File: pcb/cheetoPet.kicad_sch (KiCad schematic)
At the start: 90 parts, among them J1 bat connector, J2 USB_C_Receptacle_USB2.0_16P, Q1 FS8205A, Q2 BSS138, SW10 RESET, SW6 POWER, SW7 B, SW8 A, SW9 X, U1 USBLC6-2SC6, U10 TPS63802DLAR, U11 KLJ-01304T-08R07W, U2 MAX98357A, U3 DW01A, U4 BQ24074RGT, U5 MAX17048G_T10, U6 LSM6DSL, U7 RV-3028-C7, U8 ESP32-S3-MINI-1U, U9 WS-003DB

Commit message: pcb finished
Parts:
- removed FPC1: FPC-05FB-12PH20, EasyEDA:FPC-SMD_12P-P0.50_XUNPU_FPC-05FB-12PH20, symbol EasyEDA:FPC-05FB-12PH20
- removed J1: bat connector, Connector_PinHeader_2.00mm:PinHeader_1x02_P2.00mm_Vertical, symbol Connector:Conn_01x02_Socket
- removed SW6: POWER, EasyEDA:SW-SMD_5P-L4.2-W2.8-P1.60-LS4.6-TR, symbol EasyEDA:KMR223GLFG
- added C25: 100nF, Capacitor_SMD:C_0402_1005Metric, symbol Device:C
- added C26: 0.1uF, Capacitor_SMD:C_0402_1005Metric, symbol Device:C_Small
- added C27, C28: 22uF, Capacitor_SMD:C_0805_2012Metric, symbol Device:C
- added CN1: bat connector, EasyEDA:CONN-SMD_P2.00_S2B-PH-SM4-TB-LF-SN, symbol EasyEDA:S2B-PH-SM4-TB
- added FPC1: FPC-05F-12PH20, EasyEDA:FPC-SMD_12P-P0.50_FPC-05F-12PH20, symbol EasyEDA:FPC-05F-12PH20
- added SW1: POWER, EasyEDA:SW-SMD_LXTD-0204-034, symbol EasyEDA:LXTD-0204-034
- C1, C11, C17, C19, C5, C6, C7: LCSC Part (none) -> C1525
- C10, C14, C22, C23: LCSC Part (none) -> C45783
- C12, C2, C20, C3, C8, C9: LCSC Part (none) -> C19702
- C15, C16, C18, C21, C24: footprint Capacitor_SMD:C_0603_1608Metric -> Capacitor_SMD:C_0402_1005Metric; LCSC Part (none) -> C1525
- C4: LCSC Part (none) -> C52923
- F1: LCSC Part (none) -> C2649901
- J2: LCSC Part (none) -> C2988369
- L1: LCSC Part (none) -> C42455362
- Q1: LCSC Part (none) -> C908265
- Q2: LCSC Part (none) -> C7420339
- R1: LCSC Part (none) -> C25076
- R10: LCSC Part (none) -> C42396634
- R11: LCSC Part (none) -> C25762
- R12, R13, R15, R16, R17, R18, R22, R23, R24, R25, R26, R27, R31, R32, R35, R38, R5, R8: LCSC Part (none) -> C25744
- R19, R20: LCSC Part (none) -> C25900
- R2: LCSC Part (none) -> C11702
- R21: LCSC Part (none) -> C25077
- R28, R29, R30, R33, R34: LCSC Part (none) -> C25092
- R3, R4: LCSC Part (none) -> C25905
- R36: LCSC Part (none) -> C144750
- R37: LCSC Part (none) -> C2909393
- R6: LCSC Part (none) -> C17168
- R7: LCSC Part (none) -> C25867
- R9: LCSC Part (none) -> C852602
- TP1, TP2, TP3, TP4, TP5, TP6, TP7: now not fitted; now left out of the parts list
- U1: LCSC Part (none) -> C5180249
- U2: LCSC Part (none) -> C910544
- U3: LCSC Part (none) -> C42380662
- U4: LCSC Part (none) -> C54313
- U5: footprint MAX17048G_T10:SON50P200X200X80-9N -> Package_DFN_QFN:TDFN-8-1EP_2x2mm_P0.5mm_EP0.8x1.2mm; LCSC Part (none) -> C2682616
- U6: LCSC Part (none) -> C126672
- U7: LCSC Part (none) -> C3019759
- U8: LCSC Part (none) -> C2980299
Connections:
- net +3V3: now also C27.2, FPC1.8, FPC1.9
- net BAT+: now also CN1.1
- net BAT-: now also CN1.2
- net CHG: now also U8.27 (IO47)
- net DAC_BCLK: now also U8.21 (IO17); no longer U8.37 (IO41)
- net DAC_LRCLK: now also U8.22 (IO18); no longer U8.38 (IO42)
- net DAC_SD: now also U8.17 (IO13); no longer U8.30 (IO48)
- net EN: now also C25.1
- net GND: now also C25.2, C26.1, C27.1, C28.2, FPC1.12, FPC1.13, FPC1.14, FPC1.2, SW1.2
- net POWER: now also SW1.1
- net ROCK_L: now also U8.37 (IO41); no longer U8.21 (IO17)
- net ROCK_R: now also U8.38 (IO42); no longer U8.22 (IO18)
- net TFT_DC: now also FPC1.3
- net TFT_RES: now also FPC1.4
- net TFT_TE: now also FPC1.1
- net at R21.1: now also C26.2, C28.1, FPC1.10
- net at Q2.3 (D): now also FPC1.11
- net at R29.1: now also FPC1.5
- net at R28.1: now also FPC1.6
- net at R30.1: now also FPC1.7
- no-connect marks 27 -> 30
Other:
- moved on the sheet: R21, R26

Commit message: merged kidna with like uhhh some stuff
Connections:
- net +3V3: now also SW9.3
- net GND: no longer SW9.3
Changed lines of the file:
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@@
 	)
 	(symbol
+		(lib_id "power:+3V3")
+		(at 120.65 191.77 180)
+		(unit 1)
+		(body_style 1)
+		(exclude_from_sim no)
+		(in_bom yes)
+		(on_board yes)
+		(in_pos_files yes)
+		(dnp no)
+		(property "Reference" "#PWR053"
+			(at 120.65 187.96 0)
+			(hide yes)
+			(show_name no)
+			(do_not_autoplace no)
+			(effects
+				(font
+					(size 1.27 1.27)
+				)
+			)
+		)
+		(property "Value" "+3V3"
+			(at 120.65 195.326 0)
+			(show_name no)
+			(do_not_autoplace no)
+			(effects
+				(font
+					(size 1.27 1.27)
+				)
+			)
+		)
+		(property "Footprint" ""
+			(at 120.65 191.77 0)
+			(hide yes)
+			(show_name no)
+			(do_not_autoplace no)
+			(effects
+				(font
+					(size 1.27 1.27)
+				)
+			)
+		)
+		(property "Datasheet" ""
+			(at 120.65 191.77 0)
+			(hide yes)
+			(show_name no)
+			(do_not_autoplace no)
+			(effects
+				(font
+					(size 1.27 1.27)
+				)
+			)
+		)
+		(property "Description" "Power symbol creates a global label with name \"+3V3\""
+			(at 120.65 191.77 0)
+			(hide yes)
+			(show_name no)
+			(do_not_autoplace no)
+			(effects
+				(font
+					(size 1.27 1.27)
+				)
+			)
+		)
+		(pin "1"
+		)
+		(instances
+			(project "cheetoPet"
+				(path "/2746c69b-027c-4aec-b1d7-a024d4e17723"
+					(reference "#PWR053")
+					(unit 1)
+				)
+			)
+		)
+	)
+	(symbol
 		(lib_id "power:GND")
 		(at 359.41 143.51 0)
@@
 					(unit 1)
 				)
-			)
-		)
-	)
-	(symbol
-		(lib_id "power:GND")
-		(at 120.65 191.77 0)
-		(unit 1)
-		(body_style 1)
-		(exclude_from_sim no)
-		(in_bom yes)
-		(on_board yes)
-		(in_pos_files yes)
-		(dnp no)
-		(fields_autoplaced yes)
-		(property "Reference" "#PWR053"
-			(at 120.65 198.12 0)
-			(hide yes)
-			(show_name no)
-			(do_not_autoplace no)
-			(effects
-				(font
-					(size 1.27 1.27)
-				)
-			)
-		)
-		(property "Value" "GND"
-			(at 120.65 196.85 0)
-			(show_name no)
-			(do_not_autoplace no)
-			(effects
-				(font
-					(size 1.27 1.27)
-				)
-			)
-		)
-		(property "Footprint" ""
-			(at 120.65 191.77 0)
-			(hide yes)
-			(show_name no)
-			(do_not_autoplace no)
-			(effects
-				(font
-					(size 1.27 1.27)
-				)
-			)
-		)
-		(property "Datasheet" ""
-			(at 120.65 191.77 0)
-			(hide yes)
-			(show_name no)
-			(do_not_autoplace no)
-			(effects
-				(font
-					(size 1.27 1.27)
-				)
-			)
-		)
-		(property "Description" "Power symbol creates a global label with name \"GND\" , ground"
-			(at 120.65 191.77 0)
-			(hide yes)
-			(show_name no)
-			(do_not_autoplace no)
-			(effects
-				(font
-					(size 1.27 1.27)
-				)
-			)
-		)
-		(pin "1"
-		)
-		(instances
-			(project "cheetoPet"
-				(path "/2746c69b-027c-4aec-b1d7-a024d4e17723"
-					(reference "#PWR053")
-					(unit 1)
-				)

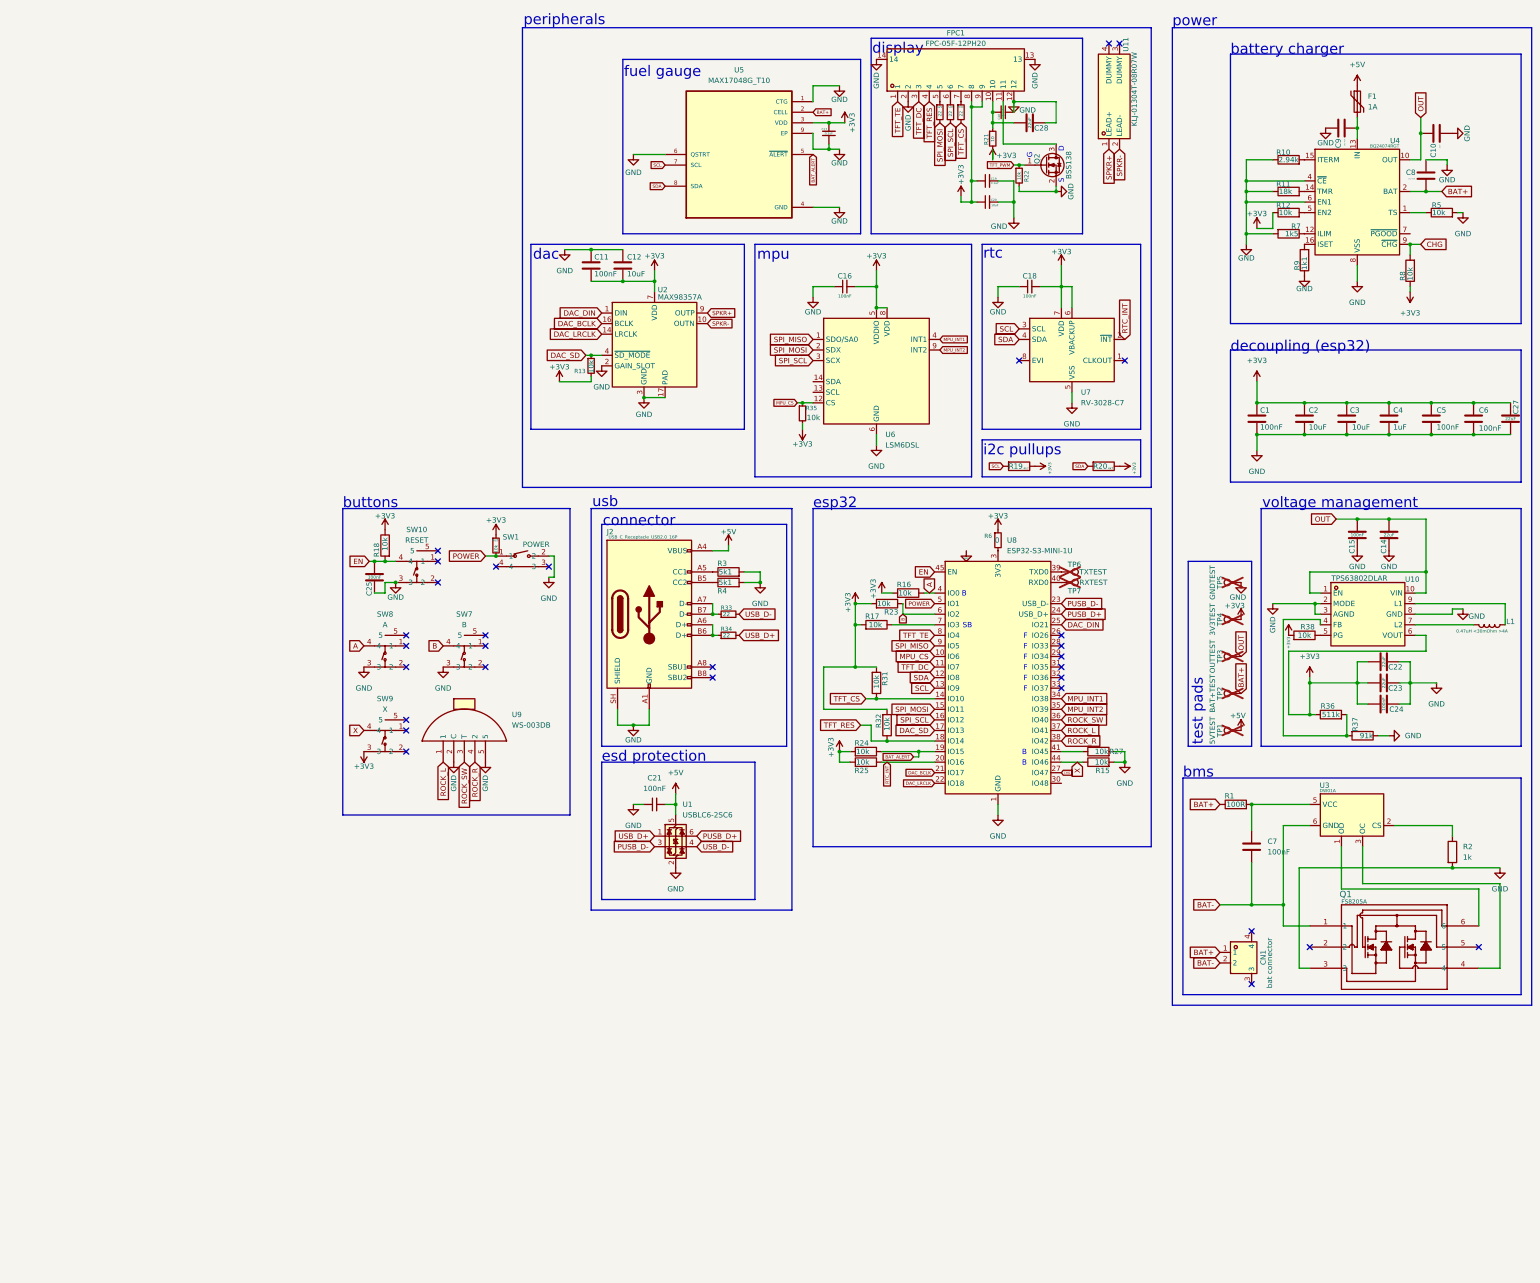
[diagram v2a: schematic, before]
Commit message: pcb v2.1 schematic finished
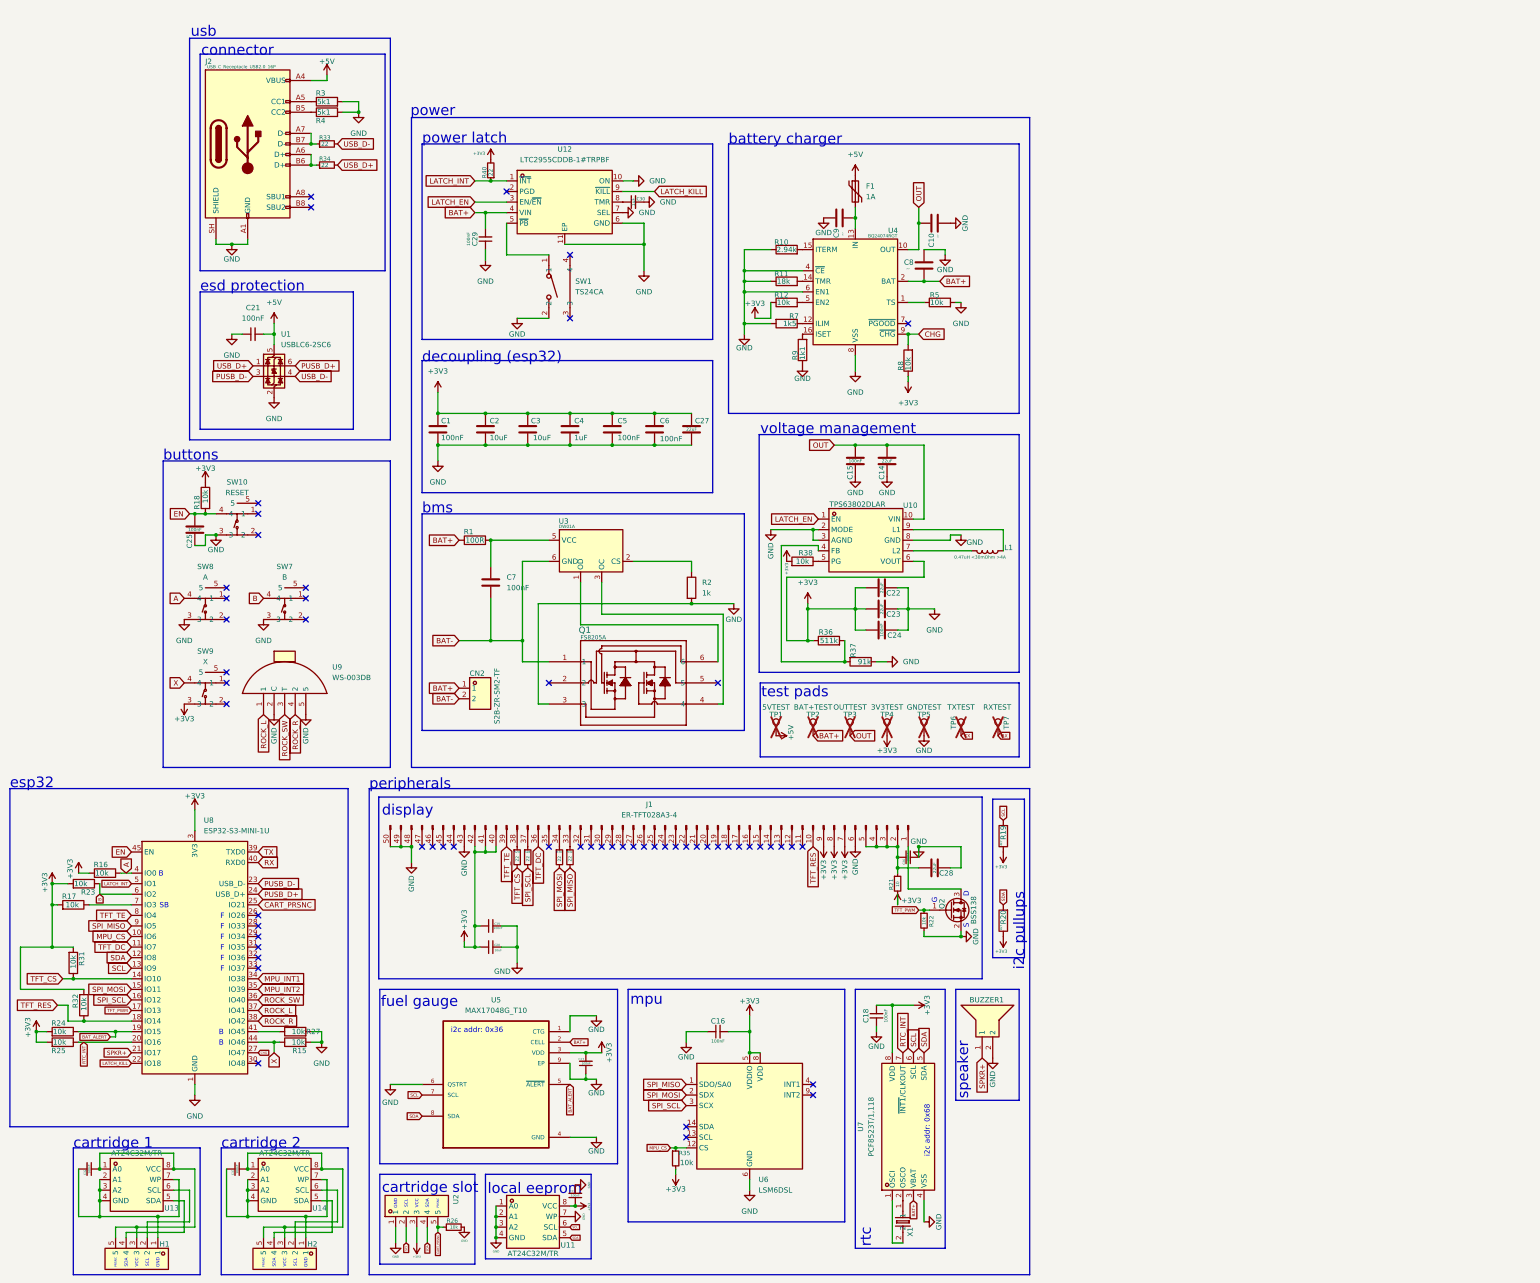
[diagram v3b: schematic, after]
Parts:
- removed C11: 100nF, Capacitor_SMD:C_0402_1005Metric, symbol Device:C
- removed C12: 10uF, Capacitor_SMD:C_0603_1608Metric, symbol Device:C
- removed CN1: bat connector, EasyEDA:CONN-SMD_P2.00_S2B-PH-SM4-TB-LF-SN, symbol EasyEDA:S2B-PH-SM4-TB
- removed FPC1: FPC-05F-12PH20, EasyEDA:FPC-SMD_12P-P0.50_FPC-05F-12PH20, symbol EasyEDA:FPC-05F-12PH20
- removed R13: 10k, Resistor_SMD:R_0402_1005Metric, symbol Device:R_Small
- removed R6: 0, Resistor_SMD:R_0402_1005Metric, symbol Device:R_Small
- removed SW1: POWER, EasyEDA:SW-SMD_LXTD-0204-034, symbol EasyEDA:LXTD-0204-034
- removed U11: KLJ-01304T-08R07W, EasyEDA:BUZ-SMD_4P-L13.0-W13.0-P11.4-BL, symbol EasyEDA:KLJ-01304T-08R07W
- removed U2: MAX98357A, Package_DFN_QFN:TQFN-16-1EP_3x3mm_P0.5mm_EP1.23x1.23mm, symbol Audio:MAX98357A
- removed U7: RV-3028-C7, Package_SON:MicroCrystal_C7_SON-8_1.5x3.2mm_P0.9mm, symbol Timer_RTC:RV-3028-C7
- added BUZZER1: CPT-9019A-SMT-TR, EasyEDA:BUZ-SMD_L9.0-W9.0_CPT-9019A-SMT-TR, symbol EasyEDA:CPT-9019A-SMT-TR
- added C29, C31, C32, C33: 100nF, Capacitor_SMD:C_0805_2012Metric, symbol Device:C_Small
- added C30: 1uF, Capacitor_SMD:C_0805_2012Metric, symbol Device:C_Small
- added CN2: S2B-ZR-SM2-TF, EasyEDA:CONN-SMD_2P-P1.50_S2B-ZR-SM2-TF-LF-SN, symbol EasyEDA:S2B-ZR-SM2-TF
- added H1, H2: HX PZ2.54-1X5P WT, EasyEDA:HDR-SMD_5P-P2.54-H-M-W12.8-N, symbol EasyEDA:HXPZ2.54-1X5PWT
- added J1: ER-TFT028A3-4, footprints:FPC-50pin,0.5Pitch, symbol Connector:Conn_01x50_Pin
- added R39, R40: 22, Resistor_SMD:R_0805_2012Metric, symbol Device:R_Small
- added SW1: TS24CA, EasyEDA:SW-SMD_2P-TS24CA, symbol EasyEDA:TS24CA
- added U11, U13, U14: AT24C32M/TR, EasyEDA:SOP-8_L4.9-W3.9-P1.27-LS6.0-BL, symbol EasyEDA:AT24C32M_TR
- added U12: LTC2955CDDB-1#TRPBF, EasyEDA:DFN-10_L3.0-W2.0-P0.50-BL-EP, symbol EasyEDA:LTC2955CDDB-1#TRPBF
- added U2: HX PM2.54-1X5P WT, EasyEDA:HDR-SMD_5P-P2.54-H-F, symbol EasyEDA:HXPM2.54-1X5PWT
- added U7: PCF8523T/1,118, EasyEDA:SOP-8_L4.9-W3.9-P1.27-LS6.0-BL, symbol EasyEDA:PCF8523T_1,118
- added X1: SC-32S32.768kHz20PPM7pF, EasyEDA:OSC-SMD_L3.2-W1.5, symbol EasyEDA:SC-32S32.768kHz20PPM7pF
- C1, C15, C16, C18, C21, C24, C25, C5, C6, C7: footprint Capacitor_SMD:C_0402_1005Metric -> Capacitor_SMD:C_0805_2012Metric; LCSC Part C1525 -> C5137467
- C10, C14, C22, C23, C27, C28: LCSC Part C45783 -> C98190
- C17, C19, C26: value 0.1uF -> 100nF; footprint Capacitor_SMD:C_0402_1005Metric -> Capacitor_SMD:C_0805_2012Metric; LCSC Part C1525 -> C5137467
- C2, C20, C3: footprint Capacitor_SMD:C_0603_1608Metric -> Capacitor_SMD:C_0805_2012Metric; LCSC Part C19702 -> C15850
- C4: footprint Capacitor_SMD:C_0402_1005Metric -> Capacitor_SMD:C_0805_2012Metric; LCSC Part C52923 -> C28323
- C8, C9: value 10uF X5R -> 10uF; footprint Capacitor_SMD:C_0603_1608Metric -> Capacitor_SMD:C_0805_2012Metric; LCSC Part C19702 -> C15850
- R1: footprint Resistor_SMD:R_0402_1005Metric -> Resistor_SMD:R_0805_2012Metric; LCSC Part C25076 -> C105577
- R10: footprint Resistor_SMD:R_0402_1005Metric -> Resistor_SMD:R_0805_2012Metric; LCSC Part C42396634 -> C865383
- R11: footprint Resistor_SMD:R_0402_1005Metric -> Resistor_SMD:R_0805_2012Metric; LCSC Part C25762 -> C17506
- R12, R15, R16, R17, R18, R22, R23, R24, R25, R26, R27, R31, R32, R35, R38, R5, R8: footprint Resistor_SMD:R_0402_1005Metric -> Resistor_SMD:R_0805_2012Metric; LCSC Part C25744 -> C2907219
- R19, R20: footprint Resistor_SMD:R_0402_1005Metric -> Resistor_SMD:R_0805_2012Metric; LCSC Part C25900 -> C2907264
- R2: footprint Resistor_SMD:R_0402_1005Metric -> Resistor_SMD:R_0805_2012Metric; LCSC Part C11702 -> C2907232
- R21: footprint Resistor_SMD:R_0402_1005Metric -> Resistor_SMD:R_0805_2012Metric; LCSC Part C25077 -> C2907220
- R28, R29, R30, R33, R34: footprint Resistor_SMD:R_0402_1005Metric -> Resistor_SMD:R_0805_2012Metric; LCSC Part C25092 -> C2907310
- R3, R4: footprint Resistor_SMD:R_0402_1005Metric -> Resistor_SMD:R_0805_2012Metric; LCSC Part C25905 -> C27834
- R36: footprint Resistor_SMD:R_0402_1005Metric -> Resistor_SMD:R_0805_2012Metric; LCSC Part C144750 -> C5159719
- R37: footprint Resistor_SMD:R_0402_1005Metric -> Resistor_SMD:R_0805_2012Metric; LCSC Part C2909393 -> C2933509
- R7: footprint Resistor_SMD:R_0402_1005Metric -> Resistor_SMD:R_0805_2012Metric; LCSC Part C25867 -> C2907216
- R9: footprint Resistor_SMD:R_0402_1005Metric -> Resistor_SMD:R_0805_2012Metric; LCSC Part C852602 -> C2933286
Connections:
- net DAC_BCLK is gone; now on net SPKR+: U8.21 (IO17)
- net DAC_SD is gone; now on net TFT_PWM: U8.17 (IO13)
- net +3V3: now also U8.3 (3V3), C31.1, J1.40 (Pin_40), J1.41 (Pin_41), J1.42 (Pin_42), J1.7 (Pin_7), J1.8 (Pin_8), J1.9 (Pin_9), R40.2, U11.8 (VCC), U2.3, U7.8 (VDD); no longer R26.1
- net BAT+: now also C29.2, CN2.1, U12.4 (VIN), U7.3 (VBAT)
- net BAT-: now also CN2.2
- net GND: now also R26.2, BUZZER1.2, C29.1, C30.2, C31.2, J1.43 (Pin_43), J1.48 (Pin_48), J1.49 (Pin_49), J1.50 (Pin_50), J1.6 (Pin_6), SW1.2, U11.1 (A0), U11.2 (A1), U11.3 (A2), U11.4 (GND), U11.7 (WP), U12.10 (ON), U12.11 (EP), U12.6 (GND), U12.7 (SEL), U2.1, U7.4 (VSS)
- net MPU_INT1: no longer U6.4 (INT1)
- net MPU_INT2: no longer U6.9 (INT2)
- net OUT: no longer U10.1 (EN)
- net RTC_INT: now also U7.7 (~{INT1}/CLKOUT)
- net SCL: now also U11.6 (SCL), U2.2, U7.6 (SCL)
- net SDA: now also U11.5 (SDA), U2.4, U7.5 (SDA)
- net SPI_MISO: now also R39.2
- net SPI_MOSI: now also R30.2; no longer R29.2
- net SPKR+: now also BUZZER1.1
- net TFT_CS: now also R29.2; no longer R30.2
- net TFT_DC: now also J1.36 (Pin_36)
- net TFT_RES: now also J1.10 (Pin_10)
- net TFT_TE: now also J1.39 (Pin_39)
- net TX: now reaches TP6.1, U8.39 (TXD0)
- net at R29.1: now also J1.38 (Pin_38)
- net at C26.2, C28.1, R21.1: now also J1.2 (Pin_2), J1.3 (Pin_3), J1.4 (Pin_4), J1.5 (Pin_5)
- net at Q2.3 (D): now also J1.1 (Pin_1)
- net at R28.1: now also J1.37 (Pin_37)
- net at R30.1: now also J1.34 (Pin_34)
- net RX: now reaches TP7.1, U8.40 (RXD0)
- net DAC_DIN renamed CART_PRSNC
- net CART_PRSNC: now also R26.1, U2.5
- net DAC_LRCLK renamed LATCH_KILL
- net LATCH_KILL: now also U12.9 (~{KILL})
- net POWER renamed LATCH_INT
- net LATCH_INT: now also R40.1, U12.1 (~{INT}); no longer R26.2
- new net: C33.1, H2.3, H2.5, U14.1 (A0), U14.8 (VCC)
- new net: C33.2, H2.1, U14.2 (A1), U14.3 (A2), U14.4 (GND), U14.7 (WP)
- new net: H2.4, U14.5 (SDA)
- new net: H2.2, U14.6 (SCL)
- new net: J1.33 (Pin_33), R39.1
- new net: U7.2 (OSCO), X1.1
- new net: U7.1 (OSCI), X1.2
- new net: C32.1, H1.3, H1.5, U13.1 (A0), U13.8 (VCC)
- new net: C32.2, H1.1, U13.2 (A1), U13.3 (A2), U13.4 (GND), U13.7 (WP)
- new net: H1.2, U13.6 (SCL)
- new net: H1.4, U13.5 (SDA)
- new net: SW1.1, U12.5 (~{PB})
- new net: C30.1, U12.8 (TMR)
- new net LATCH_EN: U10.1 (EN), U12.3 (EN/~{EN})
- no-connect marks 30 -> 58
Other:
- note added: "GND"
- note added: "PRSNC"
- note added: "SCL"
- note added: "SDA"
- note added: "VCC"
- note added: "cartridge 1"
- note added: "cartridge 2"
- note added: "cartridge slot"
- note added: "i2c addr: 0x36"
- note added: "i2c addr: 0x68"
- note added: "local eeprom"
- note added: "power latch"
- note added: "speaker"
- note removed: "dac"
- company: (none) -> fartrius industries
- title: (none) -> cheetoPet
- moved on the sheet: C1, C10, C14, C15, C16, C17, C19, C2, C20, C21, C22, C23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

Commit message: pcb tweaks
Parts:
- removed SW10: RESET, EasyEDA:SW-SMD_5P-L4.2-W2.8-P1.60-LS4.6-TR, symbol EasyEDA:KMR223GLFG
- removed SW7: B, EasyEDA:SW-SMD_5P-L4.2-W2.8-P1.60-LS4.6-TR, symbol EasyEDA:KMR223GLFG
- removed SW8: A, EasyEDA:SW-SMD_5P-L4.2-W2.8-P1.60-LS4.6-TR, symbol EasyEDA:KMR223GLFG
- removed SW9: X, EasyEDA:SW-SMD_5P-L4.2-W2.8-P1.60-LS4.6-TR, symbol EasyEDA:KMR223GLFG
- added SW1, SW2, SW3, SW4: BTN, EasyEDA:KEY-SMD_4P-L4.2-W2.8-P1.60-LS4.6, symbol EasyEDA:KMR621NGLFS
- C1, C10, C14, C15, C16, C17, C18, C19, C2, C20, C21, C22, C23, C24, C25, C26, C27, C28, C29, C3, C30, C31, C32, C33, C4, C5, C6, C7, C8, C9: footprint Capacitor_SMD:C_0805_2012Metric -> customs:C_0805_2012Metric - CUSTOM TEXT
- R1, R10, R11, R12, R15, R16, R17, R18, R19, R2, R20, R21, R22, R23, R24, R25, R26, R27, R28, R29, R3, R30, R31, R32, R33, R34, R35, R36, R37, R38, R39, R4, R40, R5, R7, R8, R9: footprint Resistor_SMD:R_0805_2012Metric -> customs:R_0805_2012Metric - CUSTOM TEXT
- renumbered SW1 to SW5
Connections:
- net +3V3: now also SW4.3
- net A: now also SW2.1
- net B: now also SW3.1
- net EN: now also SW1.1
- net GND: now also C32.2, C33.2, H1.1, H2.1, U13.2 (A1), U13.3 (A2), U13.4 (GND), U13.7 (WP), U14.2 (A1), U14.3 (A2), U14.4 (GND), U14.7 (WP), SW1.3, SW2.3, SW3.3
- net MPU_INT1: now also U6.4 (INT1)
- net MPU_INT2: now also U6.9 (INT2)
- net X: now also SW4.1
- no-connect marks 58 -> 48
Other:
- moved on the sheet: U9
